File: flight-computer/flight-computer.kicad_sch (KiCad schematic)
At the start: 22 parts, among them J1 USB_C_Receptacle_USB2.0_16P, Q1 DMN3404L, Q2 DMN3404L, SW1 SW_Push, SW2 SW_Push, U1 LMR51420X, U2 ESP32-S3-WROOM-1, U3 LSM6DSO32TR

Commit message: started pcb
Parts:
- added H1, H2, H3, H4: MountingHole_Pad, MountingHole:MountingHole_2.2mm_M2_DIN965_Pad, symbol Mechanical:MountingHole_Pad
- added J2: MEM2067-02-180-00-A, Library:CONN_MEM2067-02-180-00-A_GCT, symbol My_Library:MEM2067-02-180-00-A
- added J3: ~, Library:XT30_90, symbol My_Library:XT30
- J1: footprint (none) -> Library:CONN_USB4500_GCT
- R1: value 10k -> 100k
- SW1: value SW_Push -> Reset; footprint (none) -> Library:FSM2JMTR
- SW2: value SW_Push -> Boot; footprint (none) -> Library:FSM2JMTR
- U3: footprint LGA-14L_2P5X3X0P83_STM -> Library:LGA-14L_2P5X3X0P83_STM-M

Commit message: more routing and laying out of board
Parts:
- removed J2: MEM2067-02-180-00-A, Library:CONN_MEM2067-02-180-00-A_GCT, symbol My_Library:MEM2067-02-180-00-A
- removed J3: ~, Library:XT30_90, symbol My_Library:XT30
- added J3: Conn_01x02_Pin, TerminalBlock:TerminalBlock_Xinya_XY308-2.54-2P_1x02_P2.54mm_Horizontal, symbol Connector:Conn_01x02_Pin
- added J4, J5: Conn_01x06_Pin, Connector_JST:JST_ZH_B5B-ZR-SM4-TF_1x05-1MP_P1.50mm_Vertical, symbol Connector:Conn_01x06_Pin
- added J6: Power Connector, TerminalBlock:TerminalBlock_Xinya_XY308-2.54-2P_1x02_P2.54mm_Horizontal, symbol Connector:Conn_01x02_Pin
- added J7: Micro_SD_Card, Library:CONN_MEM2067-02-180-00-A_GCT, symbol Connector:Micro_SD_Card
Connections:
- net GND: now also H1.1, H2.1, H3.1, H4.1, J6.1 (Pin_1), J7.9 (SHIELD)
- net Remote Start 1 EN: now also J3.2 (Pin_2)
- net Remote Start 2 EN: now also J3.1 (Pin_1)
- net VBUS: now also J6.2 (Pin_2)

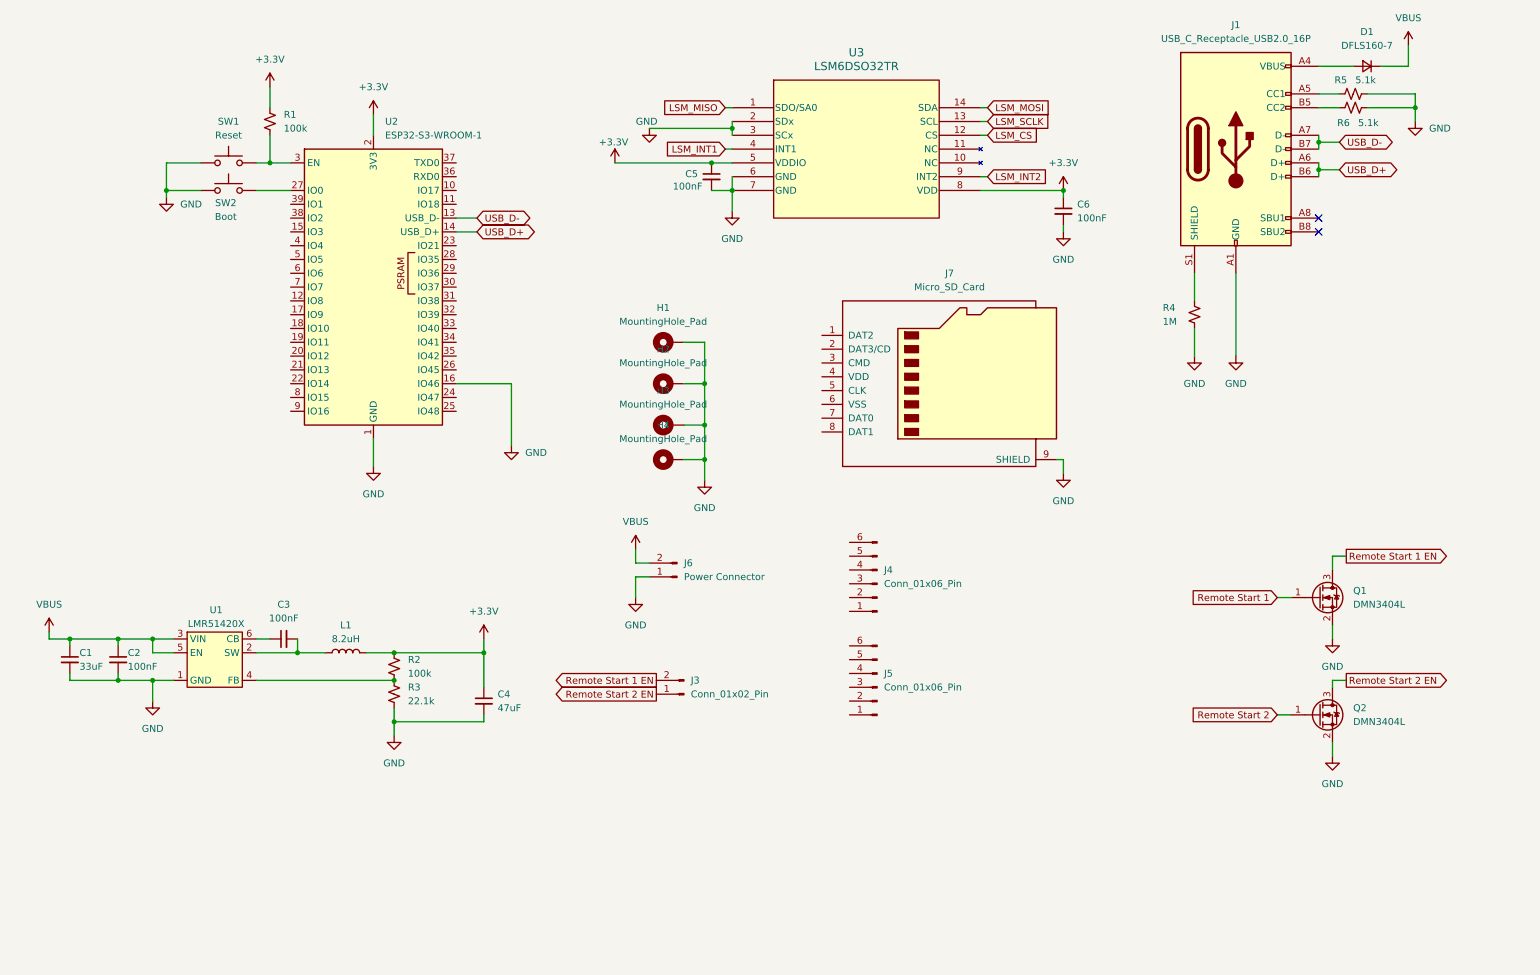
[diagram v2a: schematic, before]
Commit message: some more routing for the esp board
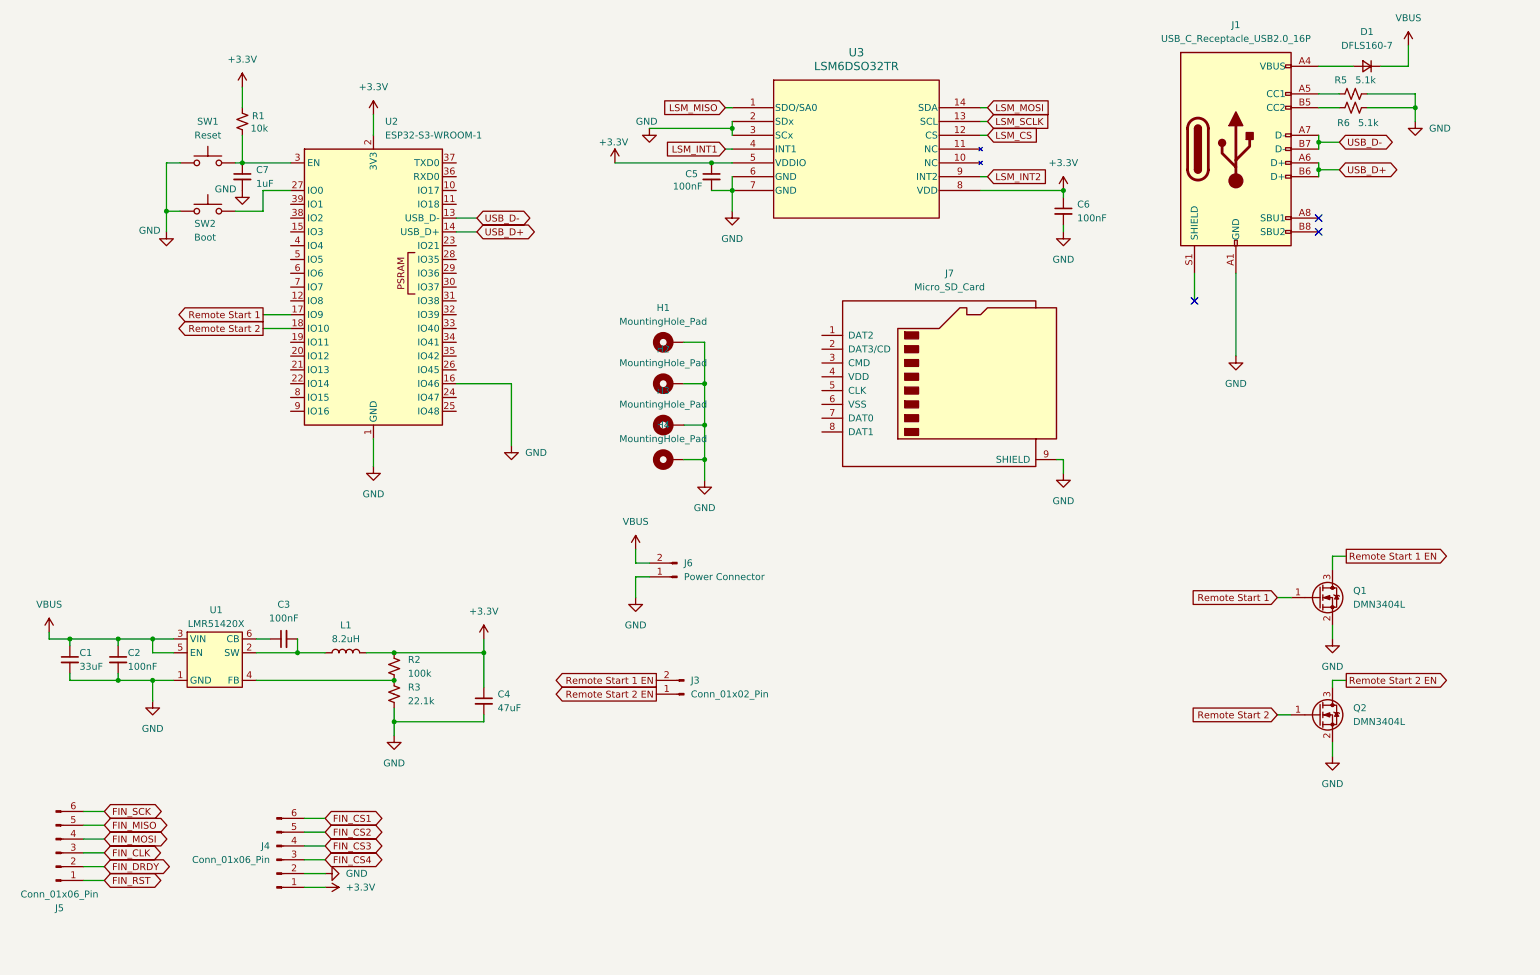
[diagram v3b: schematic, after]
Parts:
- removed R4: 1M, Resistor_SMD:R_0402_1005Metric, symbol Device:R_Small_US
- added C7: 1uF, Capacitor_SMD:C_0402_1005Metric, symbol Device:C_Small
- J1: footprint Library:CONN_USB4500_GCT -> Connector_USB:USB_C_Receptacle_Palconn_UTC16-G
- J3, J6: footprint TerminalBlock:TerminalBlock_Xinya_XY308-2.54-2P_1x02_P2.54mm_Horizontal -> Connector_PinHeader_2.54mm:PinHeader_1x02_P2.54mm_Vertical
- J4, J5: footprint Connector_JST:JST_ZH_B5B-ZR-SM4-TF_1x05-1MP_P1.50mm_Vertical -> Connector_JST:JST_ZH_S6B-ZR-SM4A-TF_1x06-1MP_P1.50mm_Horizontal
- R1: value 100k -> 10k
- U1: footprint Package_TO_SOT_SMD:SOT-23 -> Package_TO_SOT_SMD:SOT-23-6
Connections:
- net +3.3V: now also J4.1 (Pin_1)
- net GND: now also J4.2 (Pin_2), C7.2
- net Remote Start 1: now also U2.17 (IO9)
- net Remote Start 2: now also U2.18 (IO10)
- net FIN_CS4: now reaches J4.3 (Pin_3)
- net FIN_CS3: now reaches J4.4 (Pin_4)
- net FIN_CS2: now reaches J4.5 (Pin_5)
- net FIN_CS1: now reaches J4.6 (Pin_6)
- net FIN_RST: now reaches J5.1 (Pin_1)
- net FIN_DRDY: now reaches J5.2 (Pin_2)
- net FIN_CLK: now reaches J5.3 (Pin_3)
- net FIN_MOSI: now reaches J5.4 (Pin_4)
- net FIN_MISO: now reaches J5.5 (Pin_5)
- net FIN_SCK: now reaches J5.6 (Pin_6)
- net at R1.2, SW1.2, U2.3 (EN): now also C7.1
- no-connect marks 2 -> 3
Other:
- moved on the sheet: J4, J5, R1, SW1, SW2

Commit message: finish general board layout. Needs some silkscreen fixing
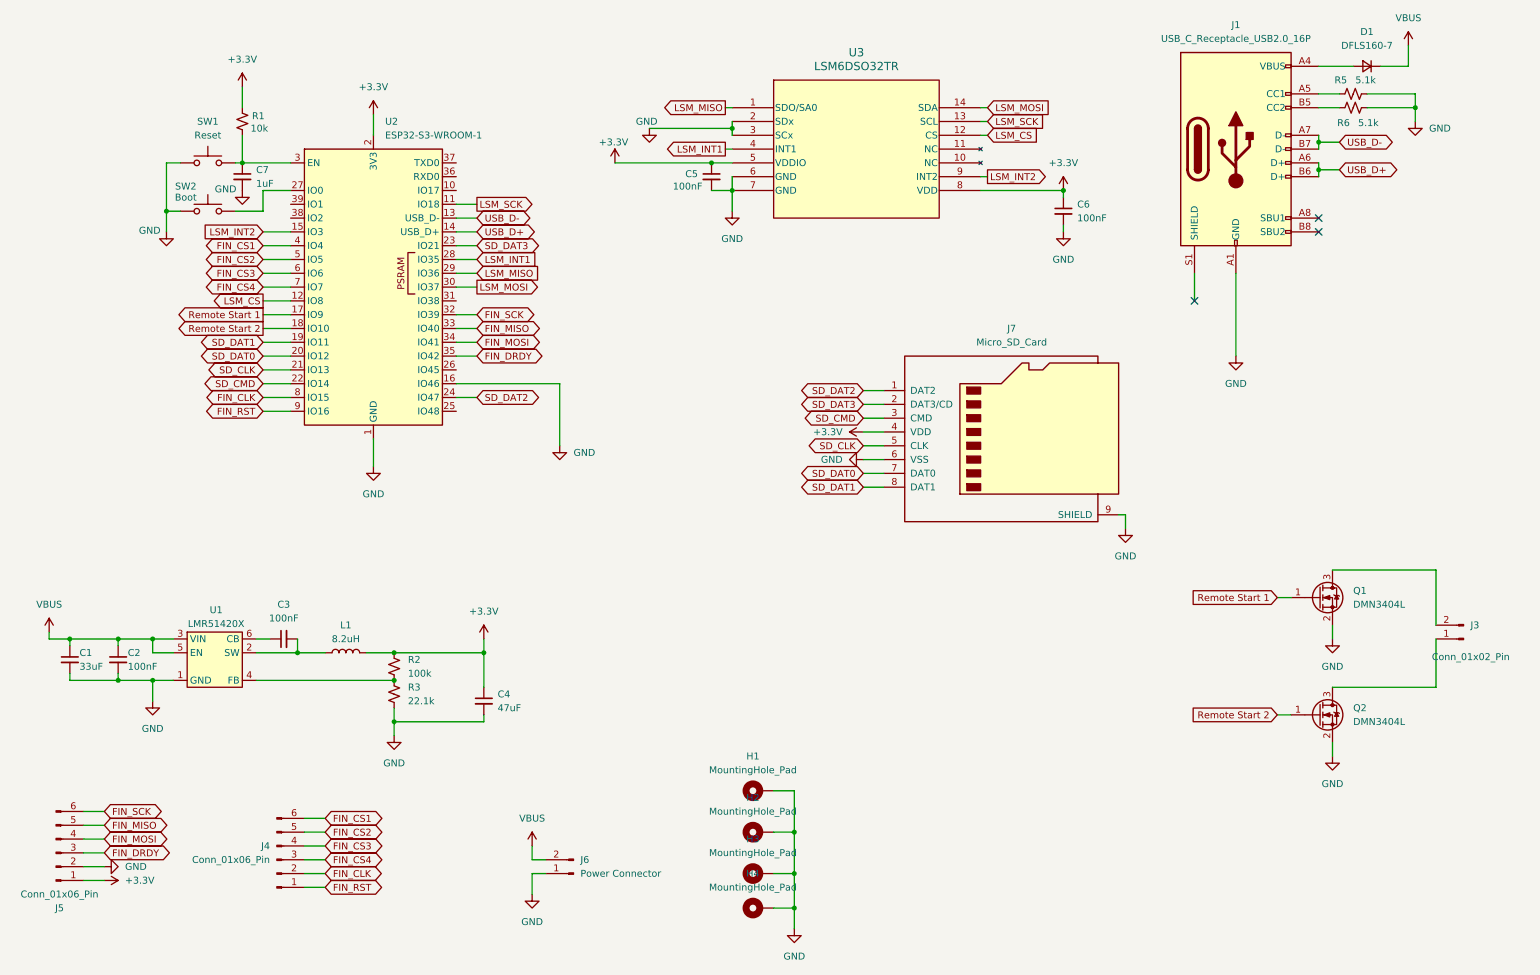
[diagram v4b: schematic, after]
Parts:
- J1: footprint Connector_USB:USB_C_Receptacle_Palconn_UTC16-G -> Connector_USB:USB_C_Receptacle_GCT_USB4105-xx-A_16P_TopMnt_Horizontal
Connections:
- net LSM_SCLK is gone; now on net LSM_SCK: U3.13 (SCL)
- net +3.3V: now also J5.1 (Pin_1), J7.4 (VDD); no longer J4.1 (Pin_1)
- net FIN_CLK: now also J4.2 (Pin_2), U2.8 (IO15); no longer J5.3 (Pin_3)
- net FIN_CS1: now also U2.4 (IO4)
- net FIN_CS2: now also U2.5 (IO5)
- net FIN_CS3: now also U2.6 (IO6)
- net FIN_CS4: now also U2.7 (IO7)
- net FIN_DRDY: now also J5.3 (Pin_3), U2.35 (IO42); no longer J5.2 (Pin_2)
- net FIN_MISO: now also U2.33 (IO40)
- net FIN_MOSI: now also U2.34 (IO41)
- net FIN_RST: now also J4.1 (Pin_1), U2.9 (IO16); no longer J5.1 (Pin_1)
- net FIN_SCK: now also U2.32 (IO39)
- net GND: now also J5.2 (Pin_2), J7.6 (VSS); no longer J4.2 (Pin_2)
- net LSM_CS: now also U2.12 (IO8)
- net LSM_INT1: now also U2.28 (IO35)
- net LSM_INT2: now also U2.15 (IO3)
- net LSM_MISO: now also U2.29 (IO36)
- net LSM_MOSI: now also U2.30 (IO37)
- net SD_DAT2: now reaches J7.1 (DAT2)
- net SD_DAT2: now also U2.24 (IO47)
- net SD_DAT3: now reaches J7.2 (DAT3/CD)
- net SD_DAT3: now also U2.23 (IO21)
- net SD_CMD: now reaches J7.3 (CMD)
- net SD_CMD: now also U2.22 (IO14)
- net SD_CLK: now reaches J7.5 (CLK)
- net SD_CLK: now also U2.21 (IO13)
- net SD_DAT0: now reaches J7.7 (DAT0)
- net SD_DAT0: now also U2.20 (IO12)
- net SD_DAT1: now reaches J7.8 (DAT1)
- net SD_DAT1: now also U2.19 (IO11)
- net LSM_SCK: now reaches U2.11 (IO18)
- net Remote Start 1 EN: no longer names the net of J3.2 (Pin_2), Q1.3 (D)
- net Remote Start 2 EN: no longer names the net of J3.1 (Pin_1), Q2.3 (D)
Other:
- moved on the sheet: H1, H2, H3, H4, J3, J6, J7

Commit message: switch out inductor and some caps
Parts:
- C5, C6: footprint Capacitor_SMD:C_0603_1608Metric -> Capacitor_SMD:C_0402_1005Metric
- L1: value 8.2uH -> 6.8uH; footprint Inductor_SMD:L_Coilcraft_XAL5050-XXX -> Library:IND_EXLA1V0505-220-R_EAT
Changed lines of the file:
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@@
 			)
 		)
-		(property "Footprint" "Capacitor_SMD:C_0603_1608Metric"
+		(property "Footprint" "Capacitor_SMD:C_0402_1005Metric"
 			(at 207.01 55.88 0)
 			(effects
@@
 			)
 		)
-		(property "Footprint" "Capacitor_SMD:C_0603_1608Metric"
+		(property "Footprint" "Capacitor_SMD:C_0402_1005Metric"
 			(at 142.24 49.53 0)
 			(effects
@@
 			)
 		)
-		(property "Value" "8.2uH"
+		(property "Value" "6.8uH"
 			(at 74.93 134.62 90)
 			(effects
@@
 			)
 		)
-		(property "Footprint" "Inductor_SMD:L_Coilcraft_XAL5050-XXX"
+		(property "Footprint" "Library:IND_EXLA1V0505-220-R_EAT"
 			(at 74.93 137.16 0)
 			(effects

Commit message: switch passive values on esp32 enable pin to be ones we already use
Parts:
- C7: value 1uF -> 100nF
- R1: value 10k -> 100k
- SW1: footprint Library:FSM2JMTR -> Jumper:SolderJumper-2_P1.3mm_Open_RoundedPad1.0x1.5mm
- SW2: footprint Library:FSM2JMTR -> Library:SW_FSM2JMTR_TEC
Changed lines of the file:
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@@
 			)
 		)
-		(property "Value" "1uF"
+		(property "Value" "100nF"
 			(at 58.42 50.8062 0)
 			(effects
@@
 			)
 		)
-		(property "Value" "10k"
+		(property "Value" "100k"
 			(at 57.404 40.64 0)
 			(effects
@@
 			)
 		)
-		(property "Footprint" "Library:FSM2JMTR"
+		(property "Footprint" "Jumper:SolderJumper-2_P1.3mm_Open_RoundedPad1.0x1.5mm"
 			(at 49.53 41.91 0)
 			(effects
@@
 			)
 		)
-		(property "Footprint" "Library:FSM2JMTR"
+		(property "Footprint" "Library:SW_FSM2JMTR_TEC"
 			(at 49.53 50.8 0)
 			(effects

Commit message: add decoupling cap right next to esp32
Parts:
- added C5: 100nF, Capacitor_SMD:C_0402_1005Metric, symbol Device:C_Small
- renumbered C7 to C3, C3 to C4, C4 to C6, C5 to C7, C6 to C8, J5 to J1, J4 to J2, J6 to J3, J7 to J4, J1 to J5, J3 to J6, R5 to R4, R6 to R5
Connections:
- net +3.3V: now also C5.1
- net GND: now also C5.2

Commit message: finishing(?) touches on flight computer board
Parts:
- removed SW1: Reset, Jumper:SolderJumper-2_P1.3mm_Open_RoundedPad1.0x1.5mm, symbol Switch:SW_Push
- removed SW2: Boot, Library:SW_FSM2JMTR_TEC, symbol Switch:SW_Push
- added SW3: SW_DIP_x02, Library:218-2LPSTR_CTS, symbol Switch:SW_DIP_x02
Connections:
- net GND: now also SW3.1, SW3.2
- net at C3.1, R1.2, U2.3 (EN): now also SW3.4
- net at U2.27 (IO0): now also SW3.3
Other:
- note added: "BOOT"
- note added: "RST"
